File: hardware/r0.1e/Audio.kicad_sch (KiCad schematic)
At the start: 85 parts, among them IC1 LM4861M, J1 Kenwood-2.5, J11 Radio_Opt, J12 Speaker, J4 CAT_TX, J5 Kenwood-3.5, J6 CAT_TX, J7 Radio, Q1 IRLML2060, Q2 BSS138, Q3 BSS138, U1 MAX9814, U6 MCP6002, U7 MCP6002

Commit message: WIP r0.1e power switch
👀
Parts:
- removed RV1: 50k, M17-SmartMic:PTR901, symbol M17-SmartMic:R_Potentiometer_Switch
- added RV4: 10k, Potentiometer_THT:Potentiometer_Alps_RK097_Single_Horizontal, symbol Device:R_Potentiometer_Small
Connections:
- net GND: now also RV4.1
- net at C10.2, R2.2, TP2.1: now also RV4.3
- net at C20.1: now also RV4.2
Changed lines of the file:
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@@
+    )
+  )
+  (symbol (lib_id "Device:R_Potentiometer_Small") (at 52.07 46.99 0) (mirror x) (unit 1)
+    (in_bom yes) (on_board yes) (dnp no) (fields_autoplaced)
+    (property "Reference" "RV4" (at 49.53 46.355 0)
+      (effects (font (size 1.27 1.27)) (justify right))
+    )
+    (property "Value" "10k" (at 49.53 48.895 0)
+      (effects (font (size 1.27 1.27)) (justify right))
+    )
+    (property "Footprint" "Potentiometer_THT:Potentiometer_Alps_RK097_Single_Horizontal" (at 52.07 46.99 0)
+      (effects (font (size 1.27 1.27)) hide)
+    )
+    (property "Datasheet" "~" (at 52.07 46.99 0)
+      (effects (font (size 1.27 1.27)) hide)
+    )
+    (pin "1")
+    (pin "2")
+    (pin "3")
+    (instances
+      (project "M17-SmartMic"
+        (path "/59592280-3207-432b-a891-cd517ec5cf12/00000000-0000-0000-0000-0000612c969e"
+          (reference "RV4") (unit 1)
+        )
+      )
     )
   )
@@
         )
       )
-    )
-  )
-  (symbol (lib_name "R_Potentiometer_Switch_1") (lib_id "M17-SmartMic:R_Potentiometer_Switch") (at 52.07 46.99 0) (mirror x) (unit 1)
-    (in_bom yes) (on_board yes) (dnp no) (fields_autoplaced)
-    (property "Reference" "RV1" (at 49.784 45.6945 0)
-      (effects (font (size 1.27 1.27)) (justify right))
-    )
-    (property "Value" "50k" (at 49.784 48.2345 0)
-      (effects (font (size 1.27 1.27)) (justify right))
-    )
-    (property "Footprint" "M17-SmartMic:PTR901" (at 52.07 46.99 0)
-      (effects (font (size 1.27 1.27)) hide)
-    )
-    (property "Datasheet" "~" (at 49.53 46.99 90)
-      (effects (font (size 1.27 1.27)) hide)
-    )
-    (pin "1")
-    (pin "2")
-    (pin "3")
-    (pin "SW1")
-    (pin "SW2")
-    (instances
-      (project "M17-SmartMic"
-        (path "/59592280-3207-432b-a891-cd517ec5cf12/00000000-0000-0000-0000-0000612c969e"
-          (reference "RV1") (unit 1)
-        )
-      )

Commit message: Gold Master r0.1e
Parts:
- removed R62: 1k, pkl_dipol:R_0603, symbol pkl_device:pkl_R_Small
- R42: value 10k -> 2k2
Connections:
- net BASEBAND_TX: now also RV3.3; no longer U6.3 (+)
- net RADIO_TX: now also C57.2; no longer RV3.2
- new net: RV3.2, U6.3 (+)
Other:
- moved on the sheet: C30, C33, C38, C51, C53, C54, C55, C57, C60, FB3, J4, J6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

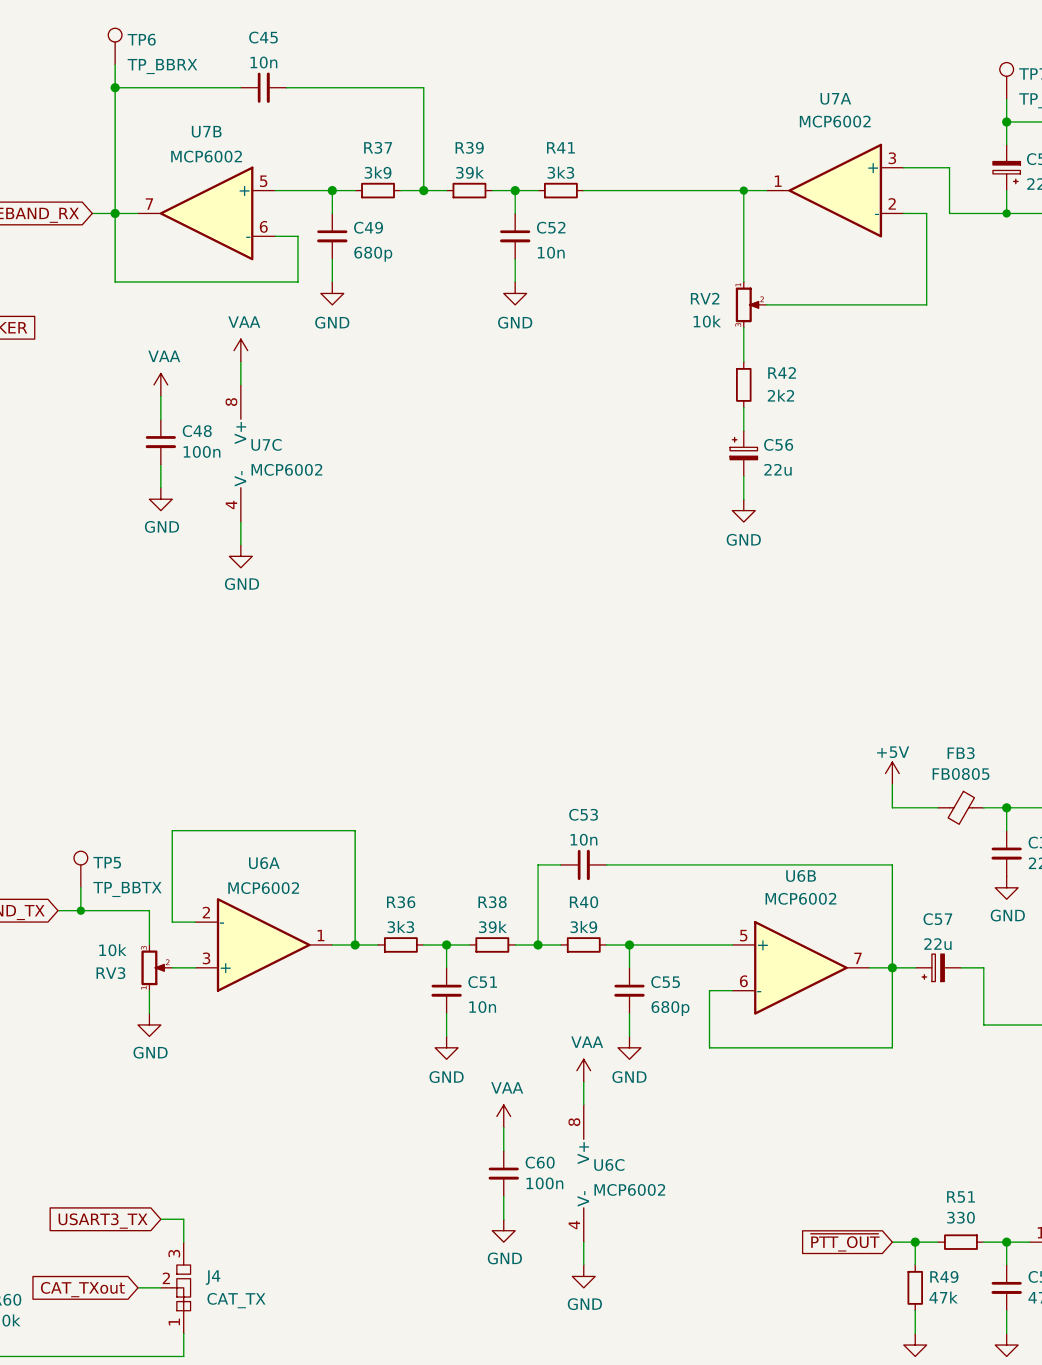
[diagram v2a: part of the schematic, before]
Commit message: Sorted some MPNs
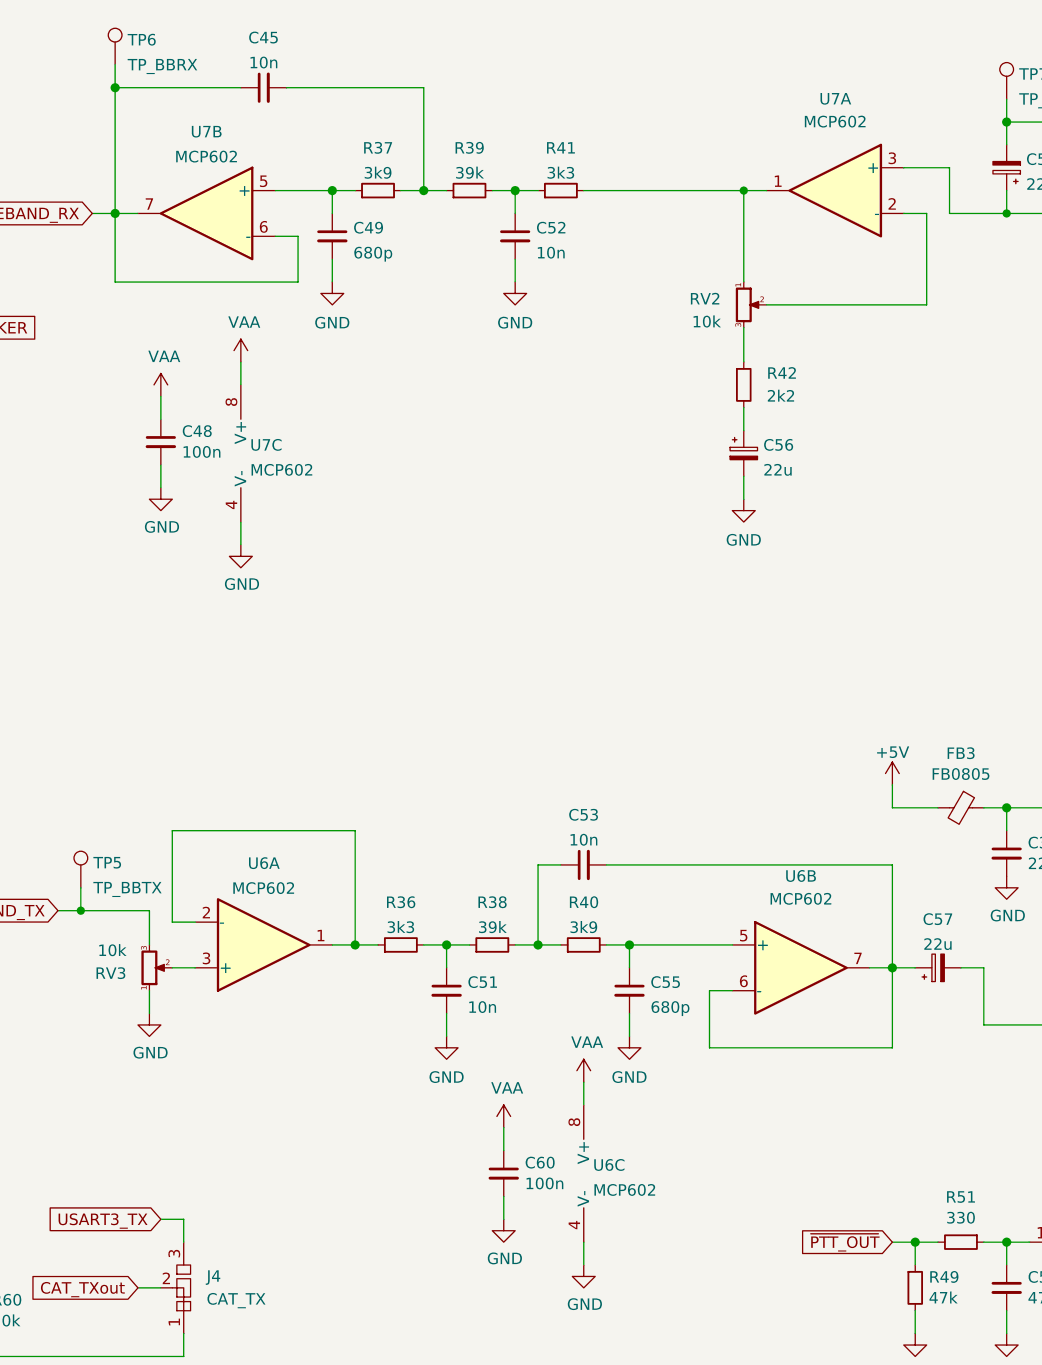
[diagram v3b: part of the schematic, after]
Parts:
- IC1: MPN (none) -> LM4861MX/NOPB; Manufacturer_Part_Number LM4861MX/NOPB -> (none)
- J1: MPN (none) -> SJ1-2503A
- Q1: MPN (none) -> IRLML2060TRPbF
- RV2: MPN (none) -> 3224W-1-103E; PartNo 3224W-1-103E -> (none)
- RV3: MPN (none) -> 3224W-1-103E
- U1: MPN (none) -> MAX9814ETD+T
- U6, U7: value MCP6002 -> MCP602; MPN (none) -> MCP602T-I/SN

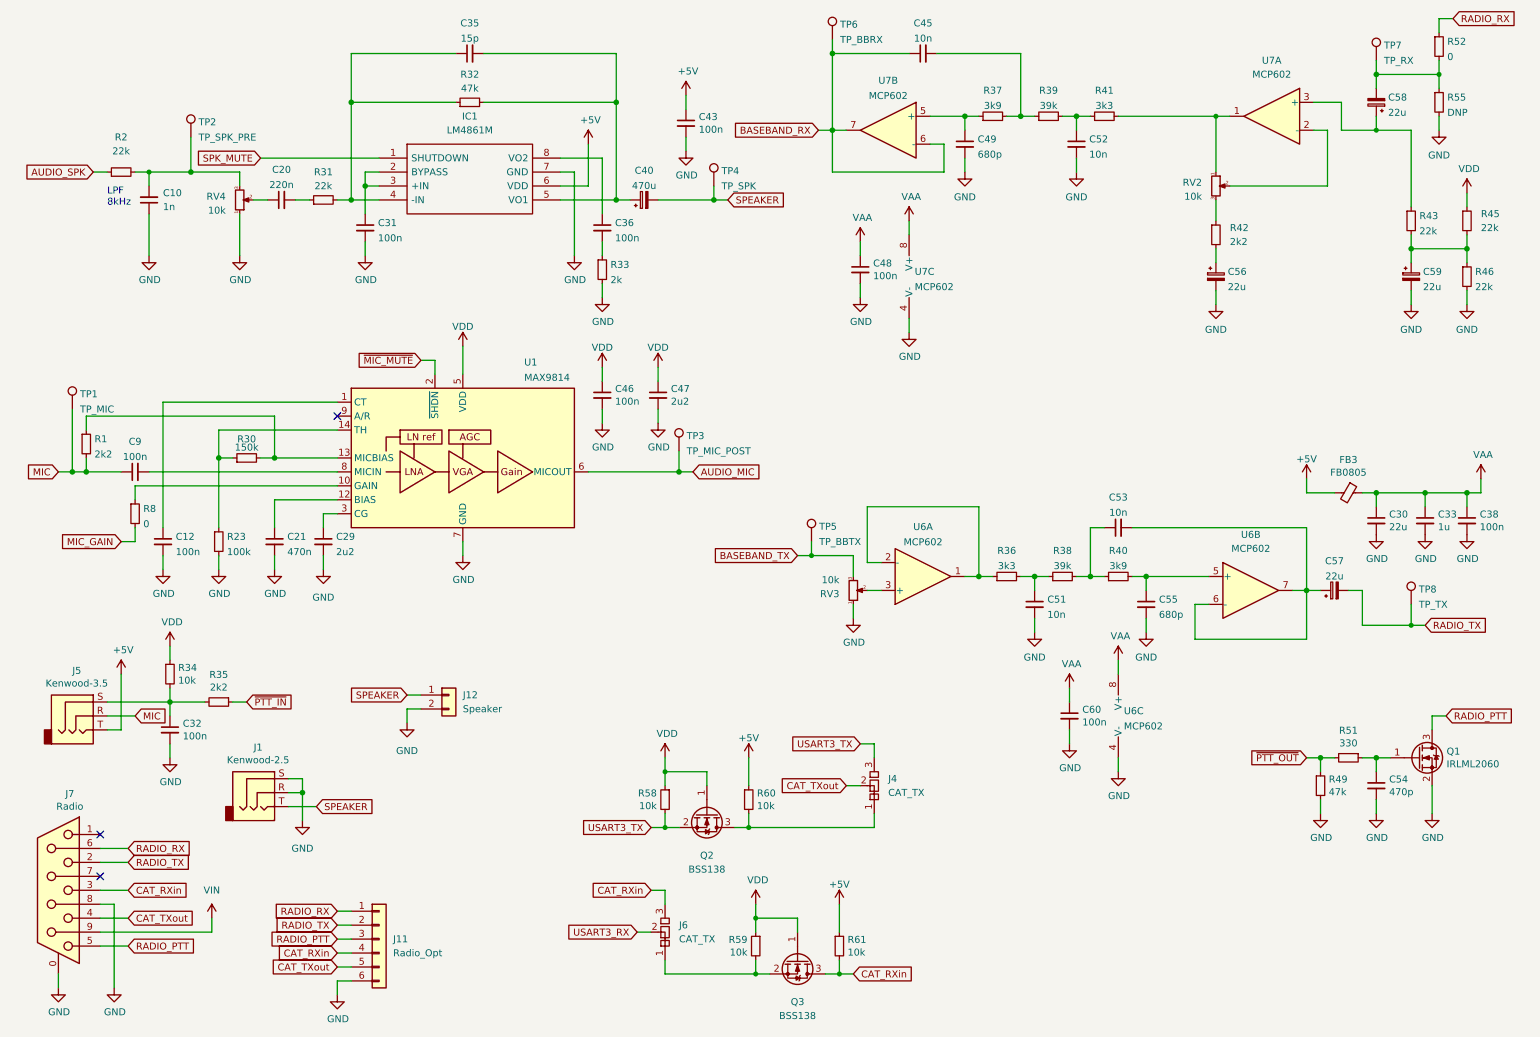
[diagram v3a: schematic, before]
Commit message: Finished MPN for r0.1e
Targeted towards LCSC/JLCPCB
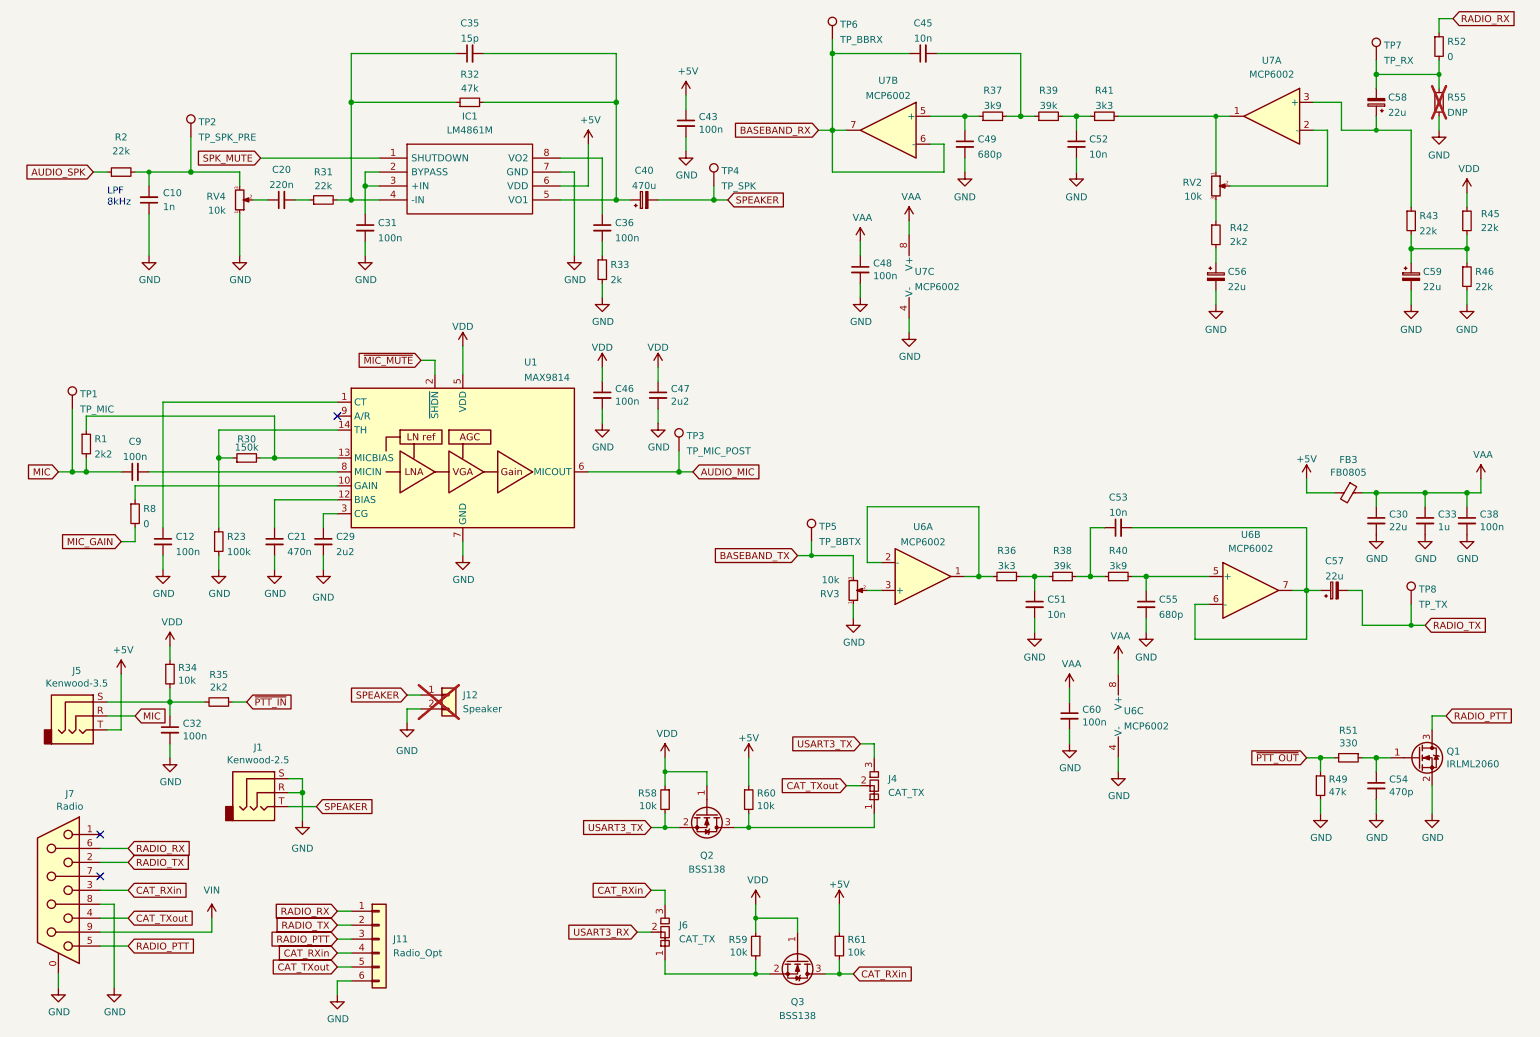
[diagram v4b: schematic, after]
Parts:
- C10: MPN (none) -> Generic C/1nF/C0G/25V/0603
- C12, C31, C32, C36, C38, C43, C46, C48, C60, C9: MPN (none) -> Generic C/100nF/C0G/25V/0603
- C20: MPN (none) -> Generic C/220nF/C0G/25V/0603
- C21: MPN (none) -> Generic C/470nF/C0G/25V/0603
- C29, C47: MPN (none) -> Generic C/2.2uF/C0G/25V/0603
- C30: MPN (none) -> Generic C/22uF/C0G/10V/0603
- C33: MPN (none) -> Generic C/1uF/C0G/25V/0603
- C35: MPN (none) -> Generic C/15pF/C0G/25V/0603
- C40: MPN (none) -> CS1A471M-CRE77
- C45, C51, C52, C53: MPN (none) -> Generic C/10nF/C0G/25V/0603
- C49, C55: MPN (none) -> Generic C/680pF/C0G/25V/0603
- C54: MPN (none) -> Generic C/470pF/C0G/25V/0603
- C56, C57, C58, C59: MPN (none) -> T491A226K006AT
- FB3: MPN (none) -> 2508056017Y2
- J1: MPN SJ1-2503A -> PJ-211A
- J11: MPN (none) -> PZ254V-11-06P
- J12: now not fitted; now left out of the parts list
- J4, J6, TP1, TP2, TP3, TP4, TP5, TP6, TP7, TP8: now left out of the parts list
- J5: MPN (none) -> PJ-3136-B
- J7: MPN (none) -> DS1037-09FNAKT74-0CC
- Q2, Q3: MPN (none) -> BSS138P,215
- R1, R35, R42: MPN (none) -> Generic R/2k2/0603
- R2, R31, R43, R45, R46: MPN (none) -> Generic R/22k/0603
- R23: MPN (none) -> Generic R/100k/0603
- R30: MPN (none) -> Generic R/150k/0603
- R32, R49: MPN (none) -> Generic R/47k/0603
- R33: MPN (none) -> Generic R/2k/0603
- R34, R58, R59, R60, R61: MPN (none) -> Generic R/10k/0603
- R36, R41: MPN (none) -> Generic R/3k3/0603
- R37, R40: MPN (none) -> Generic R/3k9/0603
- R38, R39: MPN (none) -> Generic R/39k/0603
- R51: MPN (none) -> Generic R/330/0603
- R52, R8: MPN (none) -> Generic R/0R/0603
- R55: now not fitted
- RV3: PartNo 3224W-1-103E -> (none)
- RV4: MPN (none) -> RK097111080R
- U6, U7: value MCP602 -> MCP6002; MPN MCP602T-I/SN -> MCP6002-I/SN

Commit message: r0.1e PCBA files
specifically for JLCPCB
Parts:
- C40: LCSC Part # (none) -> C116423
- C56, C57, C58, C59: LCSC Part # (none) -> C118989
- FB3: LCSC Part # (none) -> C1017
- IC1: LCSC Part # (none) -> C7958
- J1: LCSC Part # (none) -> C480265
- J11: LCSC Part # (none) -> C492405
- J5: LCSC Part # (none) -> C381131
- J7: LCSC Part # (none) -> C75749
- Q1: LCSC Part # (none) -> C67275
- Q2, Q3: LCSC Part # (none) -> C2912548
- RV2, RV3: LCSC Part # (none) -> C81348
- RV4: LCSC Part # (none) -> C470577
- U1: LCSC Part # (none) -> C41714
- U6, U7: LCSC Part # (none) -> C116706
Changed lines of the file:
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@@
       (effects (font (size 1.27 1.27)) hide)
     )
+    (property "LCSC Part #" "C1017" (at 254 100.33 0)
+      (effects (font (size 1.27 1.27)) hide)
+    )
     (pin "1")
     (pin "2")
@@
       (effects (font (size 1.27 1.27)) hide)
     )
+    (property "LCSC Part #" "C381131" (at 22.86 140.97 0)
+      (effects (font (size 1.27 1.27)) hide)
+    )
     (pin "R")
     (pin "S")
@@
       (effects (font (size 1.27 1.27)) hide)
     )
+    (property "LCSC Part #" "C67275" (at 266.7 148.59 0)
+      (effects (font (size 1.27 1.27)) hide)
+    )
     (pin "1")
     (pin "2")
@@
       (effects (font (size 1.27 1.27)) hide)
     )
+    (property "LCSC Part #" "C75749" (at 19.05 172.72 0)
+      (effects (font (size 1.27 1.27)) hide)
+    )
     (pin "0")
     (pin "1")
@@
       (effects (font (size 1.27 1.27)) hide)
     )
+    (property "LCSC Part #" "C2912548" (at 153.67 185.42 0)
+      (effects (font (size 1.27 1.27)) hide)
+    )
     (pin "1")
     (pin "2")
@@
       (effects (font (size 1.27 1.27)) hide)
     )
+    (property "LCSC Part #" "C116706" (at 170.18 34.29 0)
+      (effects (font (size 1.27 1.27)) hide)
+    )
     (pin "1")
     (pin "2")
@@
       (effects (font (size 1.27 1.27)) hide)
     )
+    (property "LCSC Part #" "C470577" (at 52.07 46.99 0)
+      (effects (font (size 1.27 1.27)) hide)
+    )
     (pin "1")
     (pin "2")
@@
       (effects (font (size 1.27 1.27)) hide)
     )
+    (property "LCSC Part #" "C2912548" (at 137.16 158.75 0)
+      (effects (font (size 1.27 1.27)) hide)
+    )
     (pin "1")
     (pin "2")
@@
       (effects (font (size 1.27 1.27)) hide)
     )
+    (property "LCSC Part #" "C116706" (at 176.53 115.57 0)
+      (effects (font (size 1.27 1.27)) hide)
+    )
     (pin "1")
     (pin "2")
@@
       (effects (font (size 1.27 1.27)) hide)
     )
+    (property "LCSC Part #" "C118989" (at 259.08 29.21 0)
+      (effects (font (size 1.27 1.27)) hide)
+    )
     (pin "1")
     (pin "2")
@@
       (effects (font (size 1.27 1.27)) hide)
     )
+    (property "LCSC Part #" "C480265" (at 55.88 154.94 0)
+      (effects (font (size 1.27 1.27)) hide)
+    )
     (pin "R")
     (pin "S")
@@
       (effects (font (size 1.27 1.27)) hide)
     )
+    (property "LCSC Part #" "C116706" (at 209.55 140.97 0)
+      (effects (font (size 1.27 1.27)) hide)
+    )
     (pin "1")
     (pin "2")
@@
       (effects (font (size 1.27 1.27)) hide)
     )
+    (property "LCSC Part #" "C118989" (at 229.87 60.96 0)
+      (effects (font (size 1.27 1.27)) hide)
+    )
     (pin "1")
     (pin "2")
@@
       (effects (font (size 1.27 1.27)) hide)
     )
+    (property "LCSC Part #" "C81348" (at 163.83 118.11 0)
+      (effects (font (size 1.27 1.27)) hide)
+    )
     (pin "1")
     (pin "2")
@@
       (effects (font (size 1.27 1.27)) hide)
     )
+    (property "LCSC Part #" "C116706" (at 176.53 60.96 0)
+      (effects (font (size 1.27 1.27)) hide)
+    )
     (pin "1")
     (pin "2")
@@
       (effects (font (size 1.27 1.27)) hide)
     )
+    (property "LCSC Part #" "C492405" (at 77.47 181.61 0)
+      (effects (font (size 1.27 1.27)) hide)
+    )
     (pin "1")
     (pin "2")
@@
       (effects (font (size 1.27 1.27)) hide)
     )
+    (property "LCSC Part #" "C7958" (at 77.47 39.37 0)
+      (effects (font (size 1.27 1.27)) hide)
+    )
     (pin "1")
     (pin "2")
@@
       (effects (font (size 1.27 1.27)) hide)
     )
+    (property "LCSC Part #" "C116423" (at 125.73 46.99 0)
+      (effects (font (size 1.27 1.27)) hide)
+    )
     (pin "1")
     (pin "2")
@@
       (effects (font (size 1.27 1.27)) hide)
     )
+    (property "LCSC Part #" "C118989" (at 251.46 118.11 0)
+      (effects (font (size 1.27 1.27)) hide)
+    )
     (pin "1")
     (pin "2")
@@
       (effects (font (size 1.27 1.27)) hide)
     )
+    (property "LCSC Part #" "C116706" (at 240.03 31.75 0)
+      (effects (font (size 1.27 1.27)) hide)
+    )
     (pin "1")
     (pin "2")
@@
       (effects (font (size 1.27 1.27)) hide)
     )
+    (property "LCSC Part #" "C81348" (at 229.87 44.45 0)
+      (effects (font (size 1.27 1.27)) hide)
+    )
     (pin "1")
     (pin "2")
@@
       (effects (font (size 1.27 1.27)) hide)
     )
+    (property "LCSC Part #" "C118989" (at 265.43 60.96 0)
+      (effects (font (size 1.27 1.27)) hide)
+    )
     (pin "1")
     (pin "2")
@@
       (effects (font (size 1.27 1.27)) hide)
     )
+    (property "LCSC Part #" "C116706" (at 236.22 118.11 0)
+      (effects (font (size 1.27 1.27)) hide)
+    )
     (pin "1")
     (pin "2")
@@
       (effects (font (size 1.27 1.27)) hide)
     )
+    (property "LCSC Part #" "C41714" (at 92.71 93.98 0)
+      (effects (font (size 1.27 1.27)) hide)
+    )
